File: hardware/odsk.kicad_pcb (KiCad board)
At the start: 2 copper layers, 64.9 x 29.8 mm, 28 parts, among them U1 TPS73133DBV, U2 PCM5102

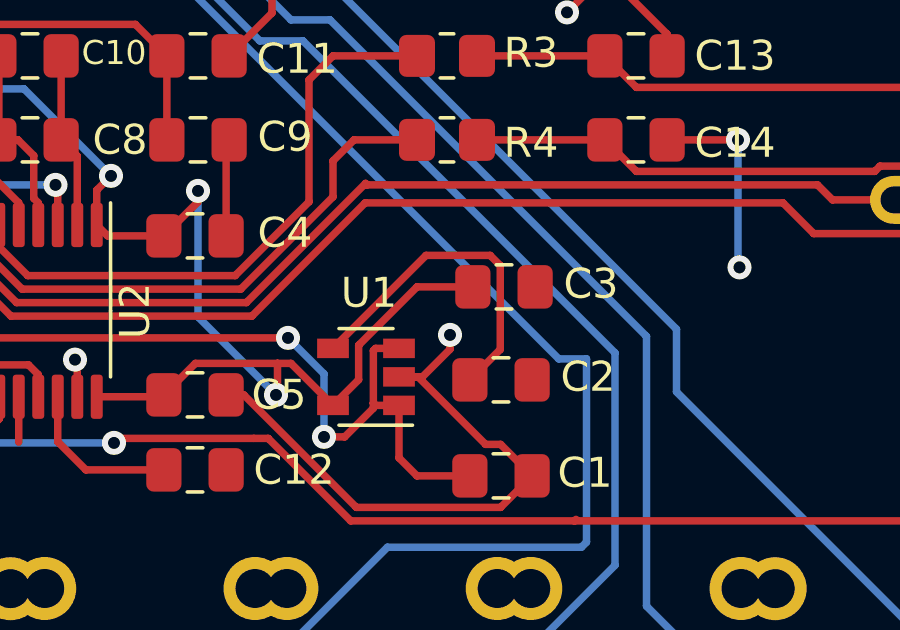
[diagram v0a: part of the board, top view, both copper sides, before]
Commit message: update cap footprint
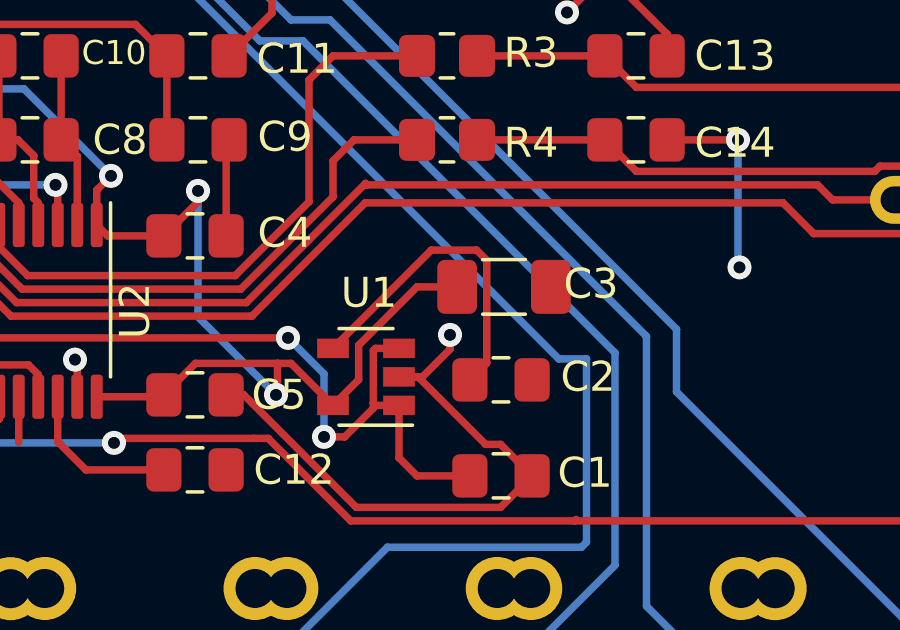
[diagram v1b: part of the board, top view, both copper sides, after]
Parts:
- C3: footprint Capacitor_SMD:C_0805_2012Metric_Pad1.18x1.45mm_HandSolder -> Capacitor_SMD:C_1206_3216Metric_Pad1.33x1.80mm_HandSolder

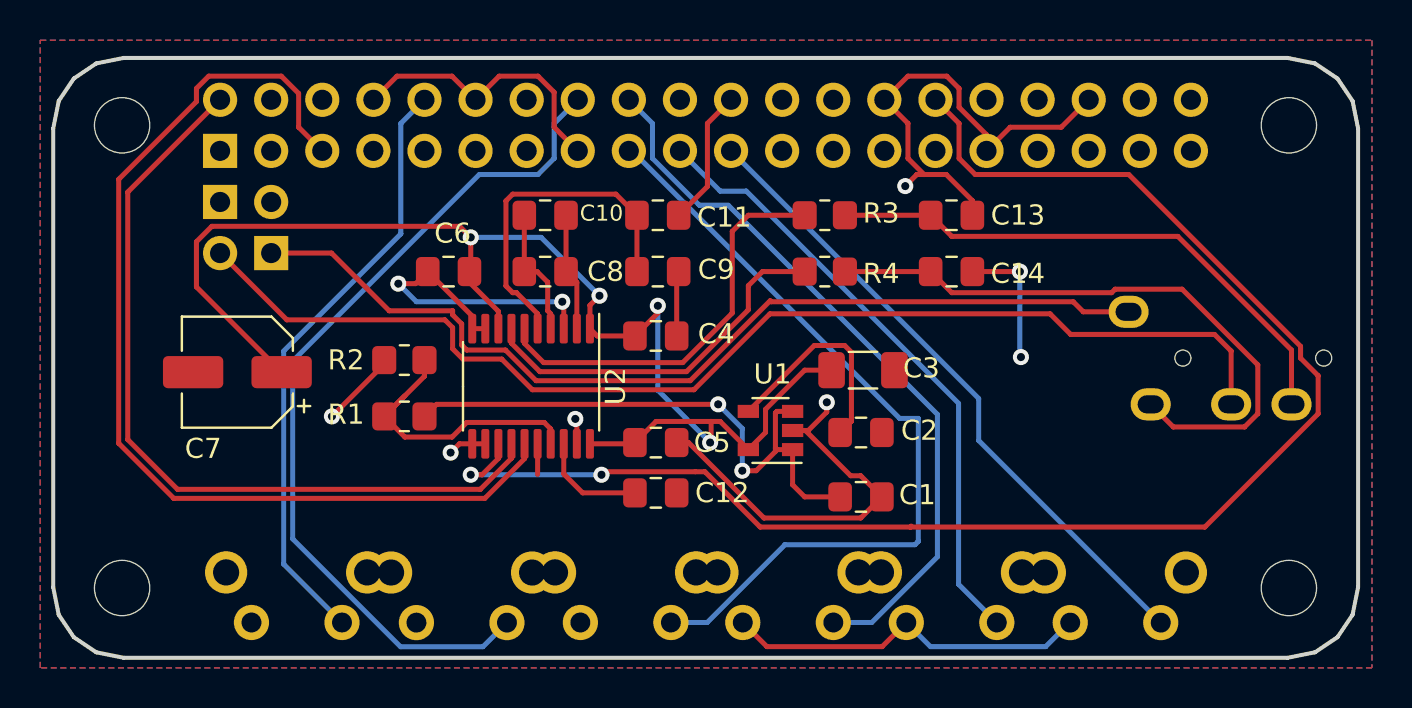
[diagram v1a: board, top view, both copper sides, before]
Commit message: update silkscreen v2.1
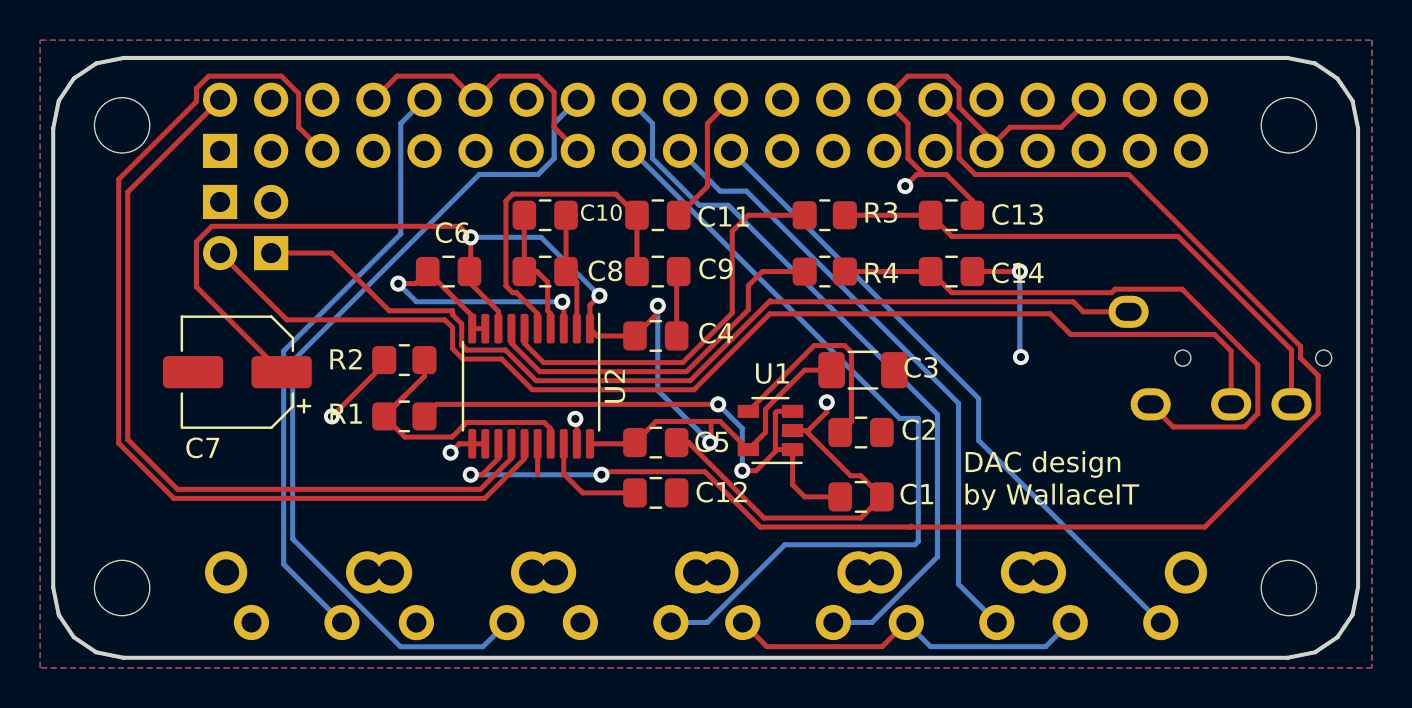
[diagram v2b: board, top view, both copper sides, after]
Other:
- net class Default removed
- board text added: "DAC design by WallaceIT"
- board text added: "autr x cyberboy666"
- board text added: "underscores.shop cyberboy666.com autr.tv"
- board text added: "v2.1"
- board text removed: "CYBERBOY666 X AUTR"
- board text removed: "v2.0"

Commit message: gpio numbering & labels
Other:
- board text added: "20 21 26 GD RUN TV"
- board text added: "5V 5V GD 14 15 18 GD 23 24 GS 25 08 07 01 GD 12 GD 16 3V 02 03 04 GD 17 27 22 3V 10 09 11 GS 00 05 06 13 19"
- board text added: "T-R-R-S"
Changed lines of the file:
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@@
     )
   )
+  (gr_line (start 173.4 140.64) (end 171.39 128.17) (layer "B.SilkS") (width 0.12))
+  (gr_line (start 191.91 129.68) (end 191.01 138.63) (layer "B.SilkS") (width 0.12))
+  (gr_line (start 171.39 128.27) (end 191.91 129.68) (layer "B.SilkS") (width 0.12))
+  (gr_line (start 191.01 138.63) (end 173.4 140.64) (layer "B.SilkS") (width 0.12))
   (gr_line (start 148.920022 145.560566) (end 148.645459 144.193881) (layer "Edge.Cuts") (width 0.2))
   (gr_line (start 149.669678 146.674262) (end 148.920022 145.560566) (layer "Edge.Cuts") (width 0.2))
@@
     (effects (font (size 1 1) (thickness 0.15)) (justify mirror))
   )
-  (gr_text "autr x cyberboy666" (at 182.12 134.78) (layer "B.SilkS")
+  (gr_text "autr x cyberboy666" (at 182.17 137.24) (layer "B.SilkS")
     (effects (font (size 1 1) (thickness 0.15)) (justify mirror))
   )
@@
     (effects (font (size 1 1) (thickness 0.15)) (justify mirror))
   )
-  (gr_text "v2.1" (at 174.27 129.69) (layer "B.SilkS")
+  (gr_text "v2.1" (at 174.32 132.15) (layer "B.SilkS")
     (effects (font (size 1 1) (thickness 0.15)) (justify mirror))
   )
-  (gr_text "odsk\n" (at 183.21 130.34) (layer "B.SilkS")
+  (gr_text "odsk\n" (at 183.26 132.8) (layer "B.SilkS")
     (effects (font (size 4 4) (thickness 0.2)) (justify mirror))
   )
   (gr_text "7/26" (at 169 143.2) (layer "B.SilkS")
     (effects (font (size 0.8 0.8) (thickness 0.15)) (justify mirror))
+  )
+  (gr_text "T-R-R-S" (at 206.6 132.9) (layer "B.SilkS")
+    (effects (font (size 1 1) (thickness 0.15)) (justify mirror))
   )
   (gr_text "11/23" (at 177.1 143.35) (layer "B.SilkS")
@@
   (gr_text "18/24" (at 185.2 143.5) (layer "B.SilkS")
     (effects (font (size 0.8 0.8) (thickness 0.15)) (justify mirror))
+  )
+  (gr_text "5V 5V GD 14 15 18 GD 23 24 GS 25 08 07 01 GD 12 GD 16\n3V 02 03 04 GD 17 27 22 3V 10 09 11 GS 00 05 06 13 19" (at 183.66 125.55) (layer "B.SilkS")
+    (effects (font (size 0.95 0.95) (thickness 0.15)) (justify mirror))
   )
   (gr_text "underscores.shop\ncyberboy666.com\nautr.tv" (at 152.9 140.81 90) (layer "B.SilkS")
@@
     (effects (font (size 1 1) (thickness 0.15)) (justify mirror))
   )
+  (gr_text "20 21\n26 GD\nRUN\nTV" (at 155.8 132.39) (layer "B.SilkS")
+    (effects (font (size 0.95 0.95) (thickness 0.15)) (justify right mirror))
+  )
   (gr_text "DAC design\nby WallaceIT" (at 193.87 138.81) (layer "F.SilkS")

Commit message: typos
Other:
- board text added: "5V 5V GD 14 15 18 GD 23 24 GD 25 08 07 01 GD 12 GD 16 3V 02 03 04 GD 17 27 22 3V 10 09 11 GS 00 05 06 13 19"
- board text added: "DAC WallaceIT"
- board text removed: "5V 5V GD 14 15 18 GD 23 24 GS 25 08 07 01 GD 12 GD 16 3V 02 03 04 GD 17 27 22 3V 10 09 11 GS 00 05 06 13 19"
- board text removed: "DAC design by WallaceIT"
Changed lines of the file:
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@@
     (effects (font (size 0.8 0.8) (thickness 0.15)) (justify mirror))
   )
-  (gr_text "5V 5V GD 14 15 18 GD 23 24 GS 25 08 07 01 GD 12 GD 16\n3V 02 03 04 GD 17 27 22 3V 10 09 11 GS 00 05 06 13 19" (at 183.66 125.55) (layer "B.SilkS")
+  (gr_text "5V 5V GD 14 15 18 GD 23 24 GD 25 08 07 01 GD 12 GD 16\n3V 02 03 04 GD 17 27 22 3V 10 09 11 GS 00 05 06 13 19" (at 183.66 125.55) (layer "B.SilkS")
     (effects (font (size 0.95 0.95) (thickness 0.15)) (justify mirror))
   )
@@
     (effects (font (size 0.95 0.95) (thickness 0.15)) (justify right mirror))
   )
-  (gr_text "DAC design\nby WallaceIT" (at 193.87 138.81) (layer "F.SilkS")
+  (gr_text "DAC\nWallaceIT" (at 193.87 138.81) (layer "F.SilkS")
     (effects (font (size 1 1) (thickness 0.15)) (justify left))
   )

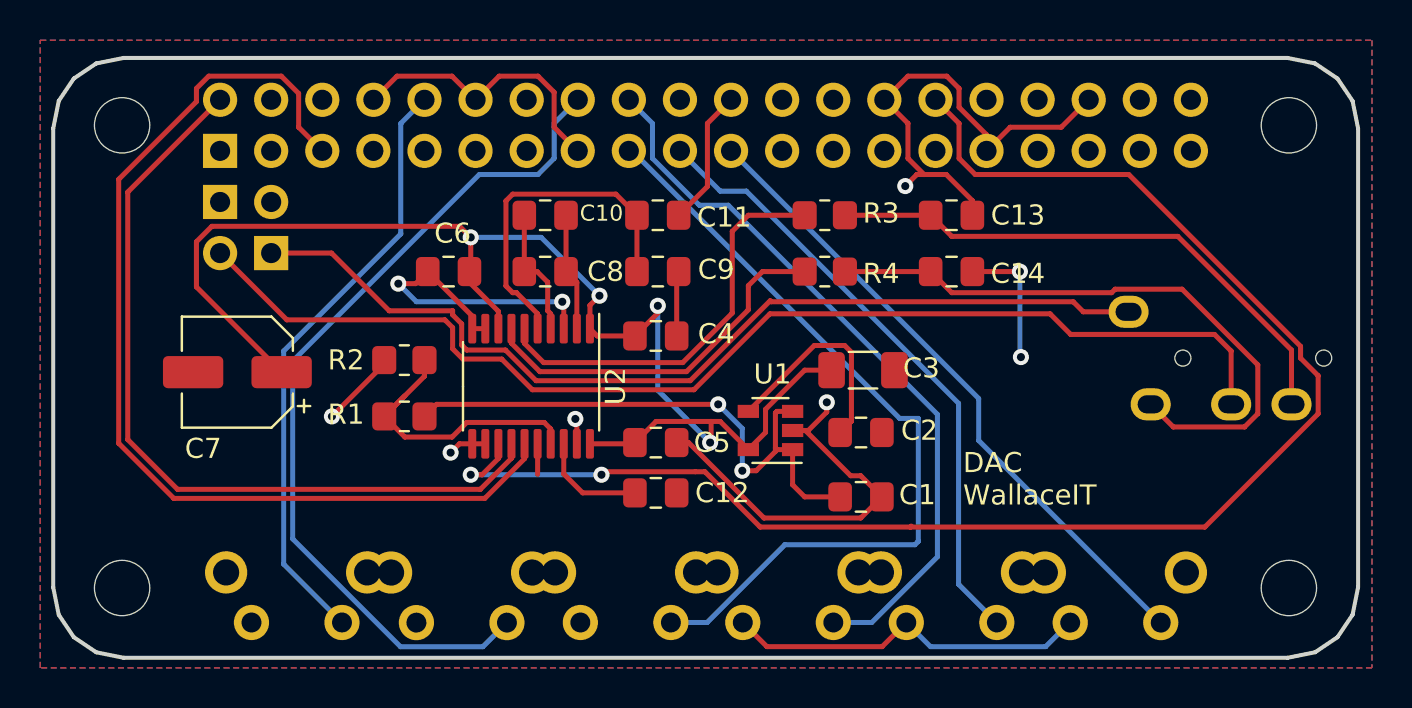
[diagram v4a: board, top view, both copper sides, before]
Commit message: [V2.2] Swap TRRS R1/R2, connect 5V, CVBS GND, reposition buttons
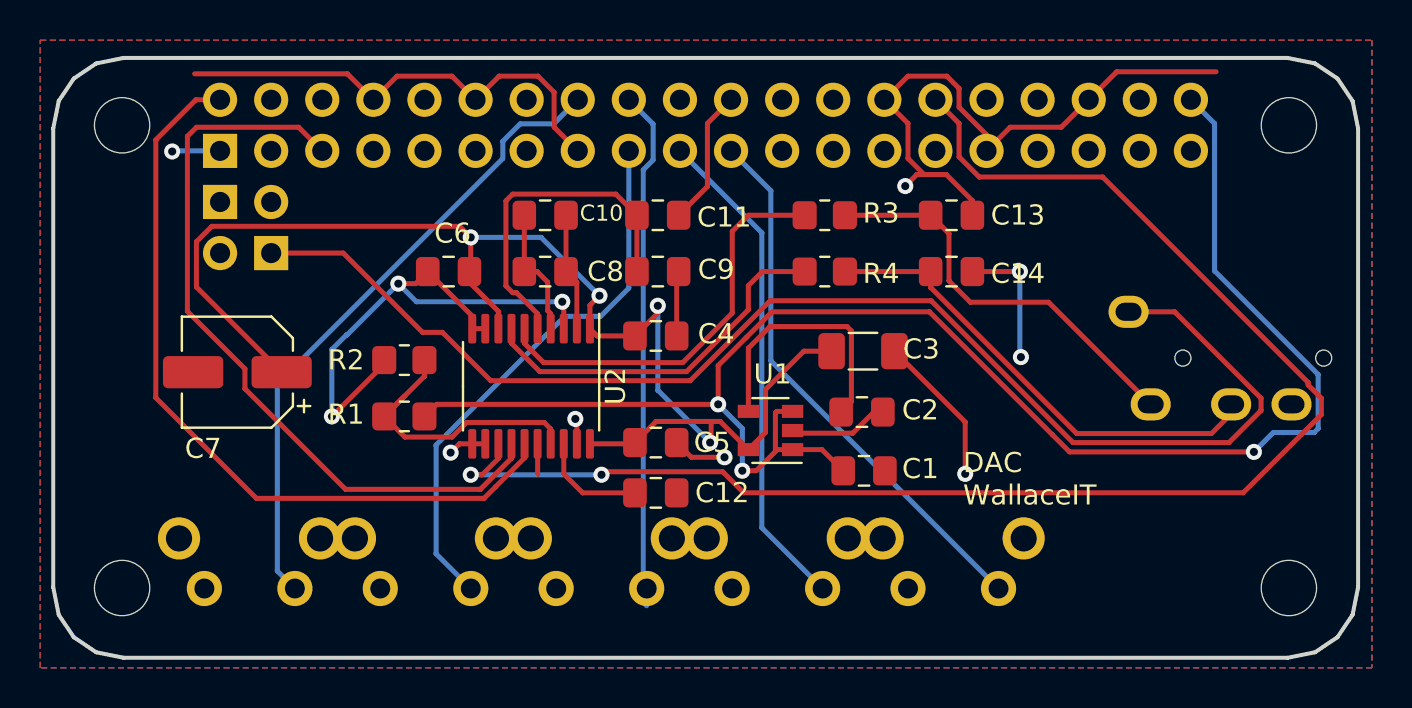
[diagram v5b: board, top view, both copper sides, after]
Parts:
- removed VOL_UP1: SW_SPST, Button_Switch_THT:SW_Tactile_SPST_Angled_PTS645Vx39-2LFS
- moved SKIP_PREV1 10.7 mm to (160.7, 144.3)
- moved SKIP_NEXT1 10.1 mm to (169.4, 144.3)
- moved OMNI1 9.43 mm to (178.1, 144.3)
- moved VOL_DOWN1 8.82 mm to (186.9, 144.3)
- moved PLAY_PAUSE1 8.24 mm to (195.6, 144.3)
- moved C1 1.30 mm to (189.0, 138.4)
- moved C2 1.02 mm to (188.8, 135.5)
- moved C3 0.94 mm to (188.9, 132.5)
- renumbered AV_OUTPUT1 to J1, PI_ZERO1 to J2
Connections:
- net /audio_dac_PCM5102a/bck renamed Net-(J2-Pad12)
- C13 pad 2: /audio_dac_PCM5102a/rout -> Net-(C13-Pad2)
- C14 pad 2: /audio_dac_PCM5102a/lrout -> Net-(C14-Pad2)
- J2 pad 1: Net-(PI_ZERO1-Pad1) -> unconnected-(J2-Pad1)
- J2 pad 10: Net-(PI_ZERO1-Pad10) -> unconnected-(J2-Pad10)
- J2 pad 11: Net-(PI_ZERO1-Pad11) -> unconnected-(J2-Pad11)
- J2 pad 13: Net-(PI_ZERO1-Pad13) -> unconnected-(J2-Pad13)
- J2 pad 15: Net-(PI_ZERO1-Pad15) -> unconnected-(J2-Pad15)
- J2 pad 16: Net-(PI_ZERO1-Pad16) -> unconnected-(J2-Pad16)
- J2 pad 17: Net-(PI_ZERO1-Pad17) -> unconnected-(J2-Pad17)
- J2 pad 18: Net-(PI_ZERO1-Pad18) -> unconnected-(J2-Pad18)
- J2 pad 2: Net-(P1-PadA4) -> +5V
- J2 pad 22: Net-(PI_ZERO1-Pad22) -> unconnected-(J2-Pad22)
- J2 pad 27: Net-(PI_ZERO1-Pad27) -> unconnected-(J2-Pad27)
- J2 pad 28: Net-(PI_ZERO1-Pad28) -> unconnected-(J2-Pad28)
- J2 pad 29: Net-(PI_ZERO1-Pad29) -> unconnected-(J2-Pad29)
- J2 pad 3: Net-(PI_ZERO1-Pad3) -> unconnected-(J2-Pad3)
- J2 pad 31: Net-(PI_ZERO1-Pad31) -> unconnected-(J2-Pad31)
- J2 pad 32: Net-(PI_ZERO1-Pad32) -> unconnected-(J2-Pad32)
- J2 pad 33: Net-(PI_ZERO1-Pad33) -> unconnected-(J2-Pad33)
- J2 pad 35: /audio_dac_PCM5102a/lrck -> Net-(J2-Pad35)
- J2 pad 36: Net-(PI_ZERO1-Pad36) -> unconnected-(J2-Pad36)
- J2 pad 37: Net-(PI_ZERO1-Pad37) -> unconnected-(J2-Pad37)
- J2 pad 38: Net-(PI_ZERO1-Pad38) -> unconnected-(J2-Pad38)
- J2 pad 4: Net-(PI_ZERO1-Pad4) -> unconnected-(J2-Pad4)
- J2 pad 40: /audio_dac_PCM5102a/din -> Net-(J2-Pad40)
- J2 pad 41: Net-(AV_OUTPUT1-PadSleeve) -> Net-(J1-PadS)
- J2 pad 42: Net-(AV_OUTPUT1-PadRing1) -> GND
- J2 pad 5: Net-(PI_ZERO1-Pad5) -> unconnected-(J2-Pad5)
- J2 pad 7: Net-(PI_ZERO1-Pad7) -> unconnected-(J2-Pad7)
- J2 pad 8: Net-(PI_ZERO1-Pad8) -> unconnected-(J2-Pad8)
- R3 pad 1: /audio_dac_PCM5102a/rout -> Net-(C13-Pad2)
- R4 pad 1: /audio_dac_PCM5102a/lrout -> Net-(C14-Pad2)
- U2 pad 14: /audio_dac_PCM5102a/din -> Net-(J2-Pad35)
- U2 pad 15: /audio_dac_PCM5102a/lrck -> Net-(J2-Pad40)
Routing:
- net Net-(J1-PadS): track 0.00 -> 66.1 mm
- net Net-(AV_OUTPUT1-PadRing1): track 58.7 -> 0.00 mm
- net +5V: track 28.7 -> 82.5 mm, vias 2 -> 3
- net /audio_dac_PCM5102a/lrck: track 51.1 -> 0.00 mm
- net Net-(AV_OUTPUT1-PadSleeve): track 47.9 -> 0.00 mm
- net /audio_dac_PCM5102a/din: track 40.2 -> 0.00 mm
- net Net-(J2-Pad40): track 0.00 -> 38.8 mm
- net Net-(J2-Pad35): track 0.00 -> 37.8 mm
- net /audio_dac_PCM5102a/lrout: track 31.1 -> 0.00 mm
- net Net-(PI_ZERO1-Pad32): track 30.1 -> 0.00 mm
- net /audio_dac_PCM5102a/rout: track 27.7 -> 0.00 mm
- net Net-(C14-Pad2): track 0.00 -> 23.9 mm
- net Net-(C13-Pad2): track 0.00 -> 20.8 mm
- net Net-(J2-Pad23): track 40.0 -> 27.5 mm
- net Net-(J2-Pad24): track 36.4 -> 25.3 mm
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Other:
- board text added: "v2.2"
- board text removed: "v2.1"
